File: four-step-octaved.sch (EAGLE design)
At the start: 36 parts, among them IC1 556, IC2 4017N, IC3 4040N, J1 BATTERY, J2 SPEAKER, U1 LM386N

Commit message: Fix missing 556 pin10 on both schematics
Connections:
- net +9V: now also IC1.RST2
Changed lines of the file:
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@@
 <wire x1="43.18" y1="88.9" x2="43.18" y2="78.74" width="0.1524" layer="91"/>
 <junction x="25.4" y="88.9"/>
-<wire x1="25.4" y1="106.68" x2="60.96" y2="106.68" width="0.1524" layer="91"/>
+<wire x1="25.4" y1="106.68" x2="27.94" y2="106.68" width="0.1524" layer="91"/>
 <junction x="25.4" y="106.68"/>
 <pinref part="IC2" gate="P" pin="VDD"/>
+<wire x1="27.94" y1="106.68" x2="60.96" y2="106.68" width="0.1524" layer="91"/>
 <wire x1="60.96" y1="106.68" x2="60.96" y2="93.98" width="0.1524" layer="91"/>
 <pinref part="C4" gate="G$1" pin="1"/>
@@
 <wire x1="-7.62" y1="20.32" x2="-7.62" y2="17.78" width="0.1524" layer="91"/>
 <wire x1="-38.1" y1="93.345" x2="-38.1" y2="33.02" width="0.1524" layer="91"/>
+<pinref part="IC1" gate="G$1" pin="RST2"/>
+<wire x1="25.4" y1="78.74" x2="27.94" y2="78.74" width="0.1524" layer="91"/>
+<wire x1="27.94" y1="78.74" x2="27.94" y2="106.68" width="0.1524" layer="91"/>
+<junction x="27.94" y="106.68"/>
 </segment>
 </net>

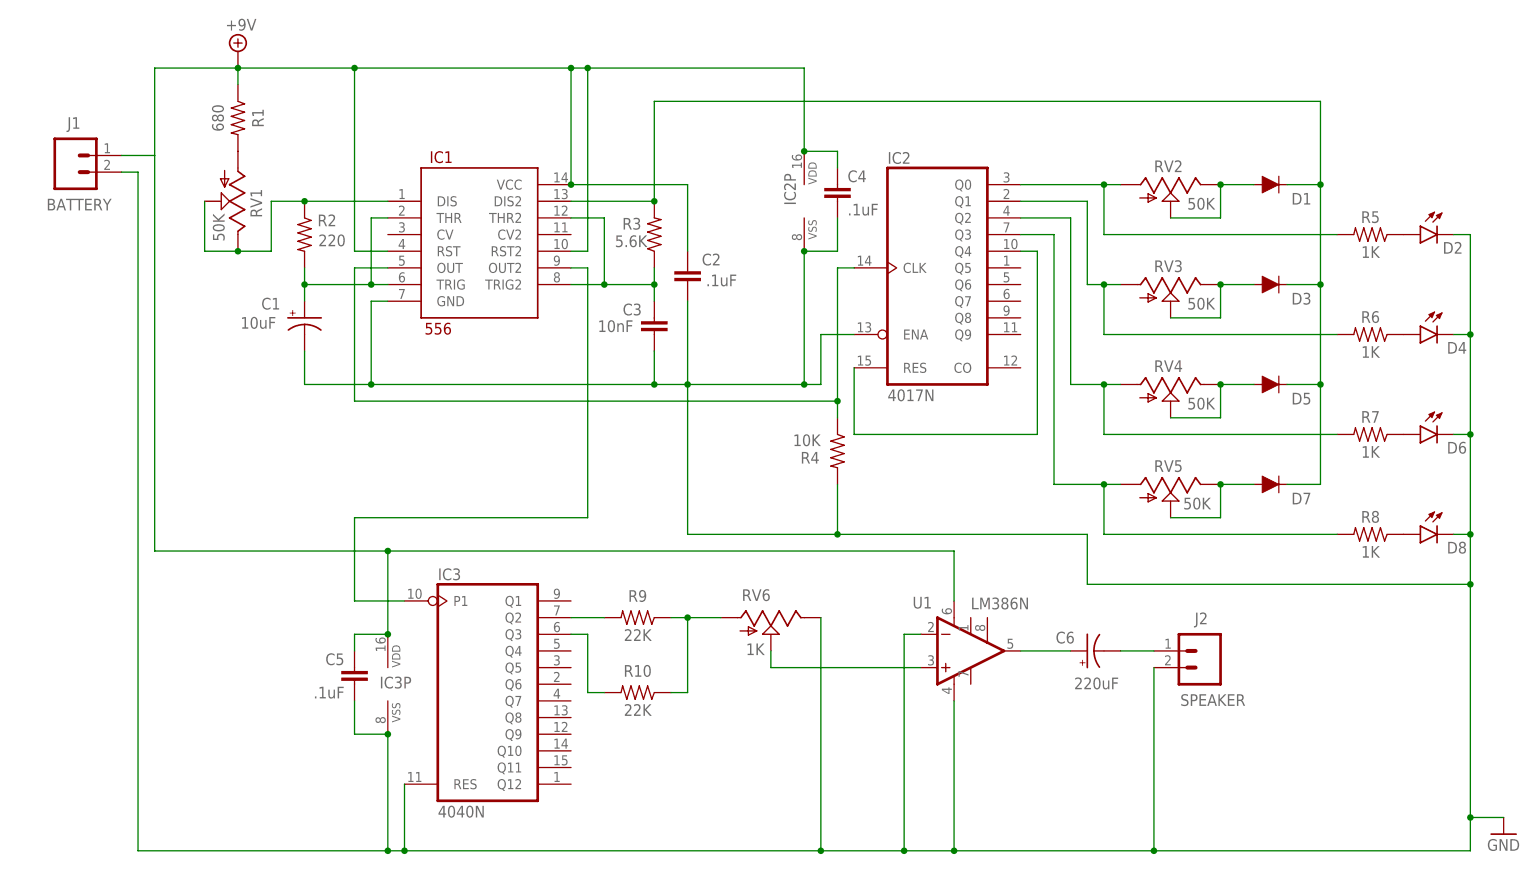
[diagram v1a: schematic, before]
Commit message: Normalize versions
* Remove previous version
* Remove version filename prefix
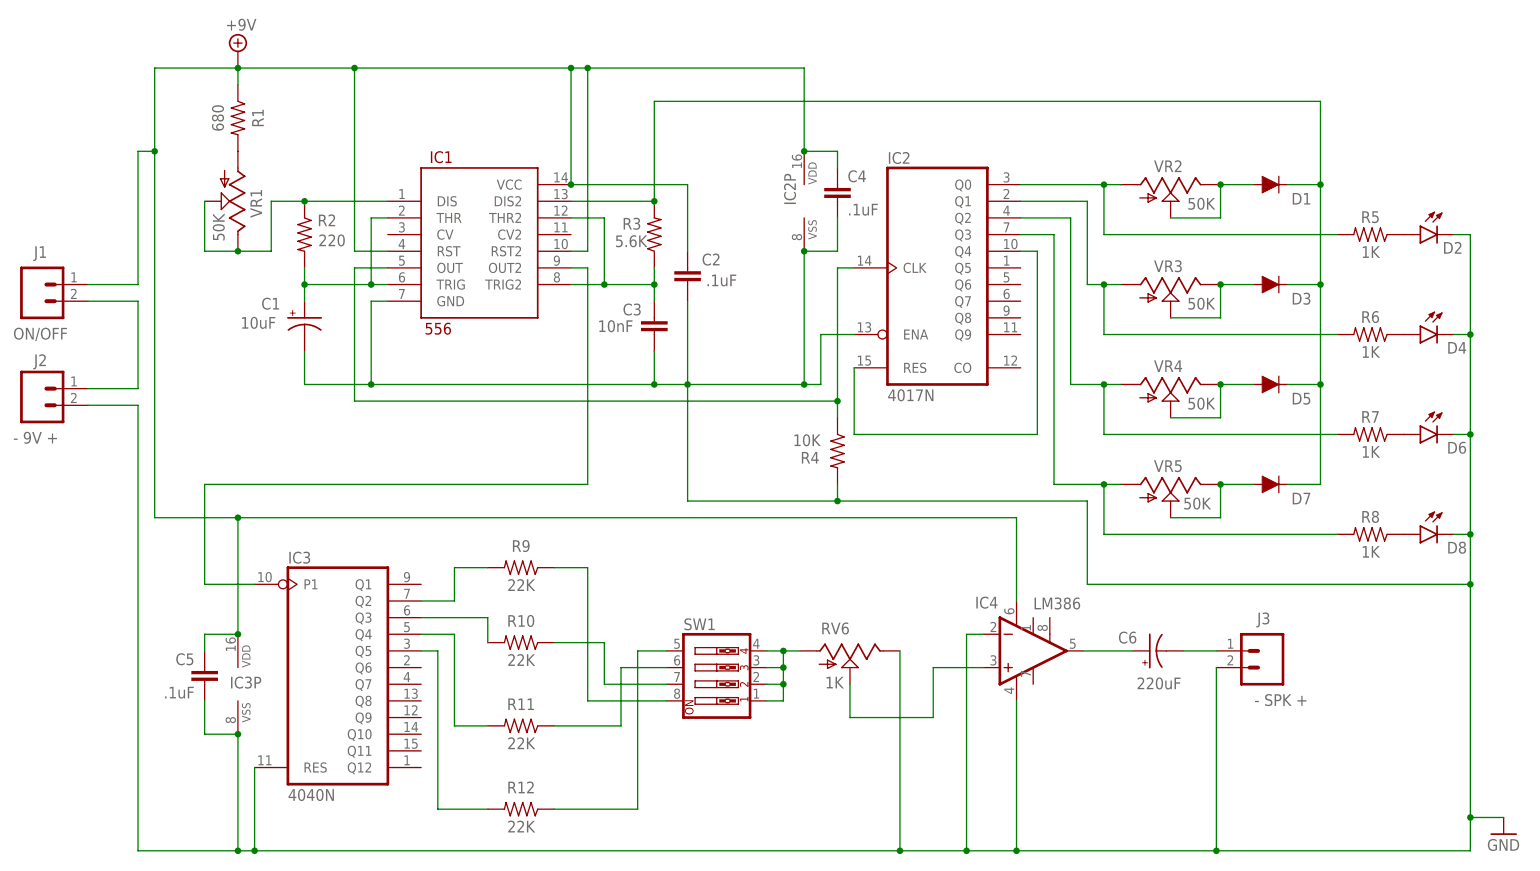
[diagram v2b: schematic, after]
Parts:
- removed U1: LM386N, SparkFun-IC-Amplifiers:LM386
- added IC4: LM386, SparkFun-IC-Amplifiers:LM386
- added J3: - SPK +, SparkFun-Connectors:CONN_02
- added R11, R12: 22K, SparkFun-Resistors:1KOHM-HORIZ-1/4W-1%
- added SW1: (no value), special:SW_DIP-4
- C6: device SparkFun-Capacitors:100UF-POLAR-RADIAL-2.5MM-25V-20% -> SparkFun-Capacitors:10UF-POLAR-RADIAL-2.5MM-25V-20%
- J1: value BATTERY -> ON/OFF
- J2: value SPEAKER -> - 9V +
- renumbered RV1 to VR1, RV2 to VR2, RV3 to VR3, RV4 to VR4, RV5 to VR5
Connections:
- new net N$21: IC3A.Q4, R11.2
- new net N$25: IC3A.Q5, R12.2
- new net N$26: R11.1, SW1.6
- new net N$29: R10.1, SW1.7
- new net N$30: R9.1, SW1.8
- new net N$31: RV6.A, SW1.1, SW1.2, SW1.3, SW1.4
- new net N$32: J1.2, J2.1
- net +9V: now also IC4.V+; no longer U1.V+
- net GND: now also IC4.-IN, IC4.V-, J3.2; no longer J1.2, U1.-IN, U1.V-
- net N$23: now also R12.1, SW1.5; no longer R10.1, R9.1, RV6.A
- net N$24: now also IC4.+IN; no longer U1.+IN
- net N$27: now also J3.1; no longer J2.1
- net N$28: now also IC4.OUT; no longer U1.OUT
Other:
- moved on the sheet: C5, C6, IC3, IC3P, J1, J2, R10, R9, RV6

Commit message: Update mixing resistor values
to what is actually in kits!
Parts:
- R10, R11, R12, R9: value 22K -> 10k
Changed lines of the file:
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@@
 <?xml version="1.0" encoding="utf-8"?>
 <!DOCTYPE eagle SYSTEM "eagle.dtd">
-<eagle version="8.2.2">
+<eagle version="9.6.2">
 <drawing>
 <settings>
 <setting alwaysvectorfont="no"/>
+<setting keepoldvectorfont="yes"/>
 <setting verticaltext="up"/>
 </settings>
-<grid distance="0.025" unitdist="inch" unit="inch" style="lines" multiple="1" display="no" altdistance="0.01" altunitdist="inch" altunit="inch"/>
+<grid distance="0.1" unitdist="inch" unit="inch" style="lines" multiple="1" display="no" altdistance="0.01" altunitdist="inch" altunit="inch"/>
 <layers>
 <layer number="1" name="Top" color="4" fill="1" visible="no" active="no"/>
@@
 <part name="D8" library="SparkFun-LED" deviceset="LED" device="3MM"/>
 <part name="C4" library="SparkFun-Capacitors" deviceset="0.1UF" device="-KIT-EZ-50V-20%" value=".1uF"/>
-<part name="R9" library="SparkFun-Resistors" deviceset="1KOHM" device="-HORIZ-1/4W-1%" value="22K"/>
-<part name="R10" library="SparkFun-Resistors" deviceset="1KOHM" device="-HORIZ-1/4W-1%" value="22K"/>
+<part name="R9" library="SparkFun-Resistors" deviceset="1KOHM" device="-HORIZ-1/4W-1%" value="10k"/>
+<part name="R10" library="SparkFun-Resistors" deviceset="1KOHM" device="-HORIZ-1/4W-1%" value="10k"/>
 <part name="RV6" library="SparkFun-Retired" deviceset="POT" device="TRIM" value="1K"/>
 <part name="C5" library="SparkFun-Capacitors" deviceset="0.1UF" device="-KIT-EZ-50V-20%" value=".1uF"/>
@@
 <part name="J3" library="SparkFun-Connectors" deviceset="CONN_02" device="" value="- SPK +"/>
 <part name="J2" library="SparkFun-Connectors" deviceset="CONN_02" device="" value="- 9V +"/>
-<part name="R11" library="SparkFun-Resistors" deviceset="1KOHM" device="-HORIZ-1/4W-1%" value="22K"/>
-<part name="R12" library="SparkFun-Resistors" deviceset="1KOHM" device="-HORIZ-1/4W-1%" value="22K"/>
+<part name="R11" library="SparkFun-Resistors" deviceset="1KOHM" device="-HORIZ-1/4W-1%" value="10k"/>
+<part name="R12" library="SparkFun-Resistors" deviceset="1KOHM" device="-HORIZ-1/4W-1%" value="10k"/>
 <part name="SW1" library="special" deviceset="SW_DIP-4" device=""/>
 <part name="J1" library="SparkFun-Connectors" deviceset="CONN_02" device="" value="ON/OFF"/>
@@
 </plain>
 <instances>
-<instance part="IC1" gate="G$1" x="10.16" y="81.28"/>
-<instance part="IC2" gate="A" x="81.28" y="76.2"/>
-<instance part="IC3" gate="A" x="-10.16" y="15.24"/>
+<instance part="IC1" gate="G$1" x="10.16" y="81.28" smashed="yes">
+<attribute name="NAME" x="3.81" y="92.202" size="1.778" layer="94"/>
+<attribute name="VALUE" x="3.048" y="66.04" size="1.778" layer="94"/>
+</instance>
+<instance part="IC2" gate="A" x="81.28" y="76.2" smashed="yes">
+<attribute name="NAME" x="73.66" y="92.075" size="1.778" layer="95"/>
+<attribute name="VALUE" x="73.66" y="55.88" size="1.778" layer="96"/>
+</instance>
+<instance part="IC3" gate="A" x="-10.16" y="15.24" smashed="yes">
+<attribute name="NAME" x="-17.78" y="31.115" size="1.778" layer="95"/>
+<attribute name="VALUE" x="-17.78" y="-5.08" size="1.778" layer="96"/>
+</instance>
 <instance part="IC4" gate="G1" x="93.345" y="17.78" smashed="yes">
 <attribute name="NAME" x="86.995" y="24.257" size="1.778" layer="95" font="vector"/>
 <attribute name="VALUE" x="95.885" y="24.13" size="1.778" layer="95" font="vector"/>
 </instance>
-<instance part="SUPPLY1" gate="G$1" x="-25.4" y="109.22"/>
-<instance part="GND1" gate="1" x="167.64" y="-10.16"/>
+<instance part="SUPPLY1" gate="G$1" x="-25.4" y="109.22" smashed="yes">
+<attribute name="VALUE" x="-27.305" y="112.395" size="1.778" layer="96"/>
+</instance>
+<instance part="GND1" gate="1" x="167.64" y="-10.16" smashed="yes">
+<attribute name="VALUE" x="165.1" y="-12.7" size="1.778" layer="96"/>
+</instance>
 <instance part="R1" gate="G$1" x="-25.4" y="99.06" smashed="yes" rot="R270">
 <attribute name="NAME" x="-23.241" y="99.06" size="1.778" layer="95" font="vector" rot="R270" align="bottom-center"/>
@@
 <attribute name="NAME" x="59.69" y="85.725" size="1.778" layer="95" rot="R90"/>
 </instance>
-<instance part="C4" gate="G$1" x="66.04" y="86.36"/>
+<instance part="C4" gate="G$1" x="66.04" y="86.36" smashed="yes">
+<attribute name="NAME" x="67.564" y="89.281" size="1.778" layer="95" font="vector"/>
+<attribute name="VALUE" x="67.564" y="84.201" size="1.778" layer="96" font="vector"/>
+</instance>
 <instance part="R9" gate="G$1" x="17.78" y="30.48" smashed="yes" rot="R180">
 <attribute name="NAME" x="17.78" y="34.671" size="1.778" layer="95" font="vector" rot="R180" align="bottom-center"/>
@@
 <attribute name="VALUE" x="64.135" y="12.065" size="1.778" layer="95"/>
 </instance>
-<instance part="IC3" gate="P" x="-25.4" y="12.7"/>
-<instance part="C5" gate="G$1" x="-30.48" y="12.7" rot="MR0"/>
+<instance part="IC3" gate="P" x="-25.4" y="12.7" smashed="yes">
+<attribute name="NAME" x="-26.67" y="12.065" size="1.778" layer="95"/>
+</instance>
+<instance part="C5" gate="G$1" x="-30.48" y="12.7" smashed="yes" rot="MR0">
+<attribute name="NAME" x="-32.004" y="15.621" size="1.778" layer="95" font="vector" rot="MR0"/>
+<attribute name="VALUE" x="-32.004" y="10.541" size="1.778" layer="96" font="vector" rot="MR0"/>
+</instance>
 <instance part="C6" gate="G$1" x="113.665" y="17.78" smashed="yes" rot="R90">
 <attribute name="NAME" x="111.76" y="20.701" size="1.778" layer="95" font="vector" rot="R180"/>
@@
 <attribute name="VALUE" x="17.78" y="-9.906" size="1.778" layer="96" font="vector" rot="R180" align="top-center"/>
 </instance>
-<instance part="SW1" gate="A" x="47.625" y="15.24"/>
+<instance part="SW1" gate="A" x="47.625" y="15.24" smashed="yes">
+<attribute name="NAME" x="42.545" y="20.955" size="1.778" layer="95"/>
+<attribute name="VALUE" x="42.545" y="5.08" size="1.778" layer="96"/>
+</instance>
 <instance part="J1" gate="G$1" x="-55.88" y="73.66" smashed="yes" rot="MR180">
 <attribute name="VALUE" x="-59.69" y="67.056" size="1.778" layer="96" font="vector" rot="MR180"/>

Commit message: Denote alternate 4040 chip
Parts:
- IC3: value 4040N -> CD4040 / MC14040
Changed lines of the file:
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@@
 <part name="IC1" library="SparkFun-IC-Special-Function" deviceset="556" device="" value="556"/>
 <part name="IC2" library="40xx" deviceset="4017" device="N"/>
-<part name="IC3" library="40xx" deviceset="4040" device="N"/>
+<part name="IC3" library="40xx" deviceset="4040" device="N" value="CD4040 / MC14040"/>
 <part name="IC4" library="SparkFun-IC-Amplifiers" deviceset="LM386" device="" value="LM386"/>
 <part name="SUPPLY1" library="supply2" deviceset="+9V" device=""/>

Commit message: Fix errant RV->VR name
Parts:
- renumbered RV6 to VR6
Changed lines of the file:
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@@
 <part name="R9" library="SparkFun-Resistors" deviceset="1KOHM" device="-HORIZ-1/4W-1%" value="10k"/>
 <part name="R10" library="SparkFun-Resistors" deviceset="1KOHM" device="-HORIZ-1/4W-1%" value="10k"/>
-<part name="RV6" library="SparkFun-Retired" deviceset="POT" device="TRIM" value="1K"/>
+<part name="VR6" library="SparkFun-Retired" deviceset="POT" device="TRIM" value="1K"/>
 <part name="C5" library="SparkFun-Capacitors" deviceset="0.1UF" device="-KIT-EZ-50V-20%" value=".1uF"/>
 <part name="C6" library="SparkFun-Capacitors" deviceset="10UF-POLAR" device="-RADIAL-2.5MM-25V-20%" value="220uF"/>
@@
 <attribute name="VALUE" x="17.78" y="15.494" size="1.778" layer="96" font="vector" rot="R180" align="top-center"/>
 </instance>
-<instance part="RV6" gate="G$1" x="67.945" y="17.78" smashed="yes" rot="R270">
+<instance part="VR6" gate="G$1" x="67.945" y="17.78" smashed="yes" rot="R270">
 <attribute name="NAME" x="63.5" y="20.32" size="1.778" layer="95"/>
 <attribute name="VALUE" x="64.135" y="12.065" size="1.778" layer="95"/>
@@
 <net name="N$24" class="1">
 <segment>
-<pinref part="RV6" gate="G$1" pin="S"/>
+<pinref part="VR6" gate="G$1" pin="S"/>
 <wire x1="67.945" y1="12.7" x2="67.945" y2="7.62" width="0.1524" layer="91"/>
 <pinref part="IC4" gate="G1" pin="+IN"/>
@@
 <wire x1="-22.86" y1="-12.7" x2="-22.86" y2="0" width="0.1524" layer="91"/>
 <wire x1="-25.4" y1="-12.7" x2="-22.86" y2="-12.7" width="0.1524" layer="91"/>
-<pinref part="RV6" gate="G$1" pin="E"/>
+<pinref part="VR6" gate="G$1" pin="E"/>
 <wire x1="75.565" y1="17.78" x2="75.565" y2="-12.7" width="0.1524" layer="91"/>
 <wire x1="-22.86" y1="-12.7" x2="75.565" y2="-12.7" width="0.1524" layer="91"/>
@@
 <wire x1="55.245" y1="15.24" x2="57.785" y2="15.24" width="0.1524" layer="91"/>
 <junction x="57.785" y="15.24"/>
-<pinref part="RV6" gate="G$1" pin="A"/>
+<pinref part="VR6" gate="G$1" pin="A"/>
 <wire x1="57.785" y1="17.78" x2="60.325" y2="17.78" width="0.1524" layer="91"/>
 <junction x="57.785" y="17.78"/>
